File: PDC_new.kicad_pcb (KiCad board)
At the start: 2 copper layers, 156.5 x 145.5 mm, 83 parts, among them J1 Conn_01x02_Pin, J10 Conn_01x02_Pin, J11 XT90PW(2+2)-M.G.Y, J12 Conn_01x02_Pin, J13 Conn_01x02_Pin, J14 Conn_01x02_Pin, J15 Conn_01x02_Pin, J2 Conn_01x02_Pin, J3 Conn_01x02_Pin, J4 Conn_01x02_Pin, J5 Conn_01x02_Pin, J6 Conn_01x02_Pin, J7 Conn_01x02_Pin, J8 Conn_01x02_Pin, J9 Conn_01x02_Pin, Q2 IRF540NSTRLPBF, U1 TPSI3050QDWZRQ1, U10 LM393LVDR, U11 IPB017N10N5ATMA1, U12 IPB017N10N5ATMA1, U14 IPB017N10N5ATMA1, U2 TPSI3050QDWZRQ1, U4 74HC74, U5 URB4805LD-60WR3, U6 IPB017N10N5ATMA1, U7 TLC555CDR, U8 SN74HC08D, U9 SN74HC14DR

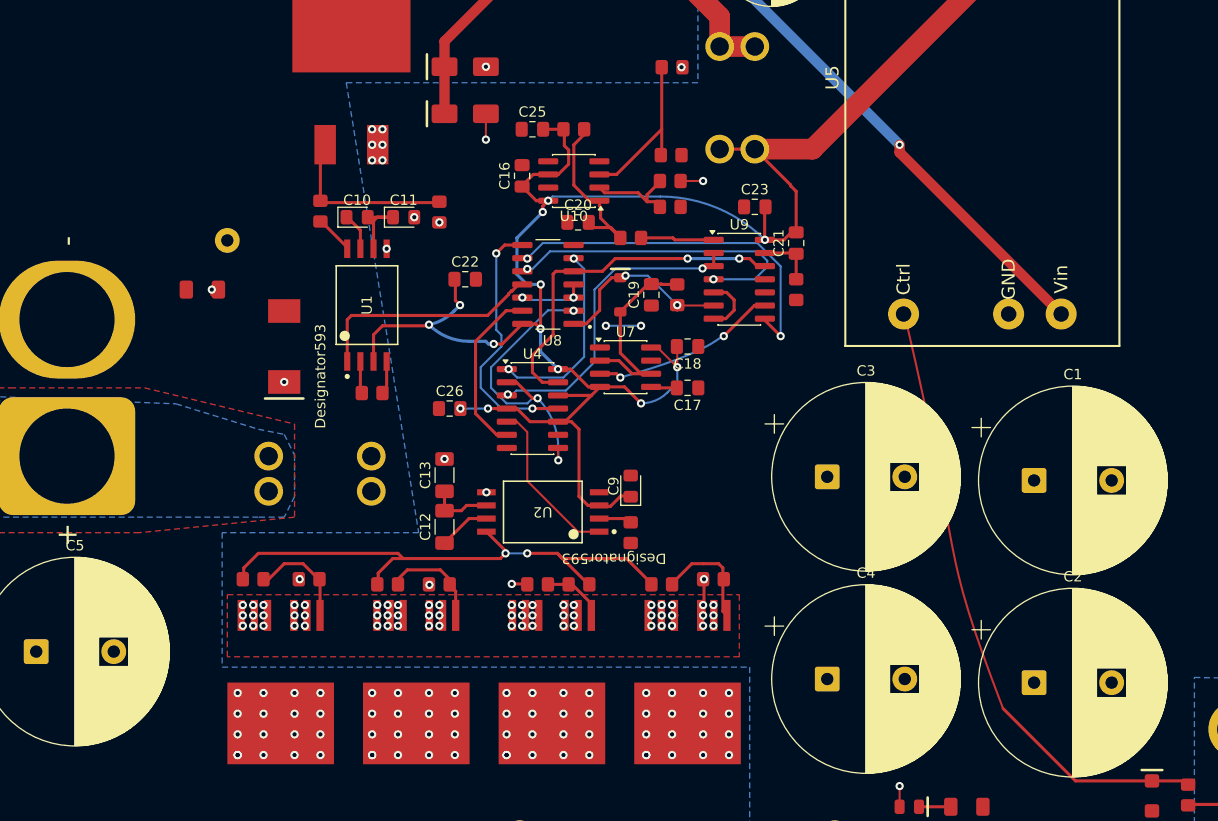
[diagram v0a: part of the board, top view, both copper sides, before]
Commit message: updated layout
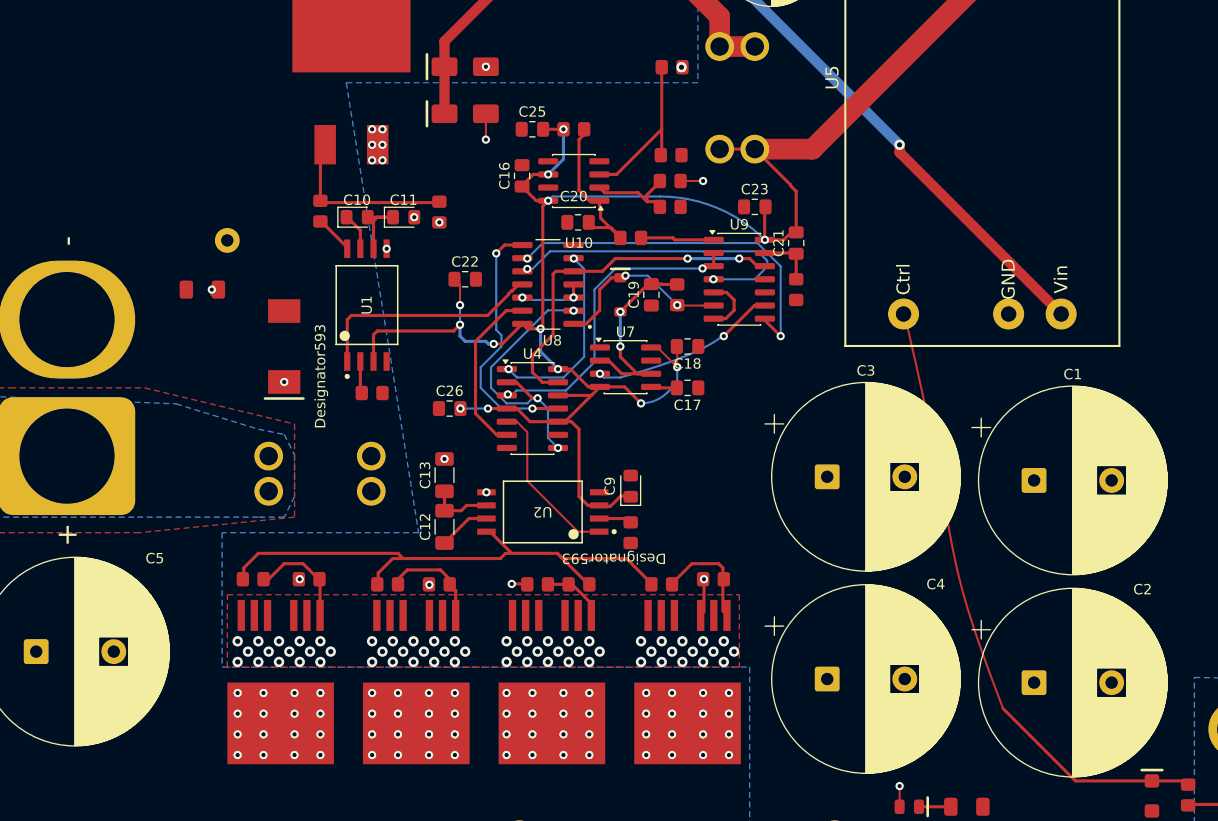
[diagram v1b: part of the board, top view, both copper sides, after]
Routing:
- net GND: track 12.2 -> 6.28 mm, vias 2 -> 0
- net /+5V: track 203.0 -> 198.6 mm
- net /BUS+: track 15.6 -> 11.8 mm
- net /FAULT_N: track 28.9 -> 27.1 mm
- net /TIMER_RC: track 20.5 -> 21.7 mm, vias 0 -> 2
- net /GATE_U11: track 6.19 -> 5.05 mm
- net /GATE_U6: track 10.8 -> 10.2 mm
- net /GATE_MAIN: track 54.0 -> 54.5 mm, vias 2 -> 0
- net /BATT+: vias 72 -> 68
